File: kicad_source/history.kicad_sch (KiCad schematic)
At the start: 0 parts

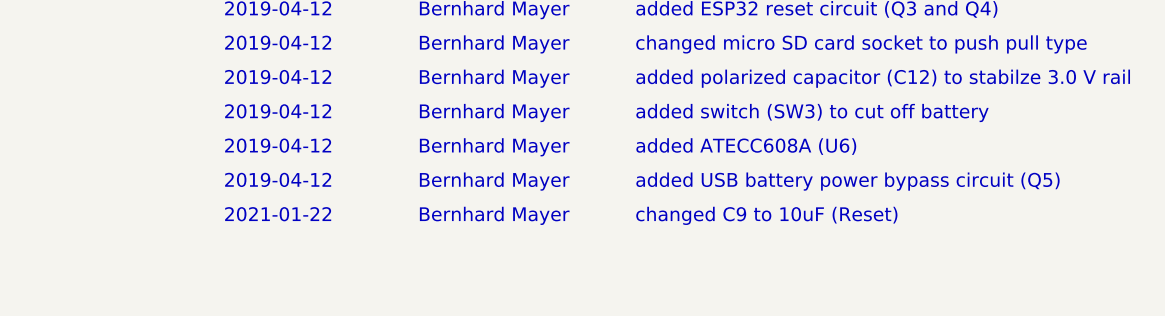
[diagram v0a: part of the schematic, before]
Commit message: added pull up on BOOT
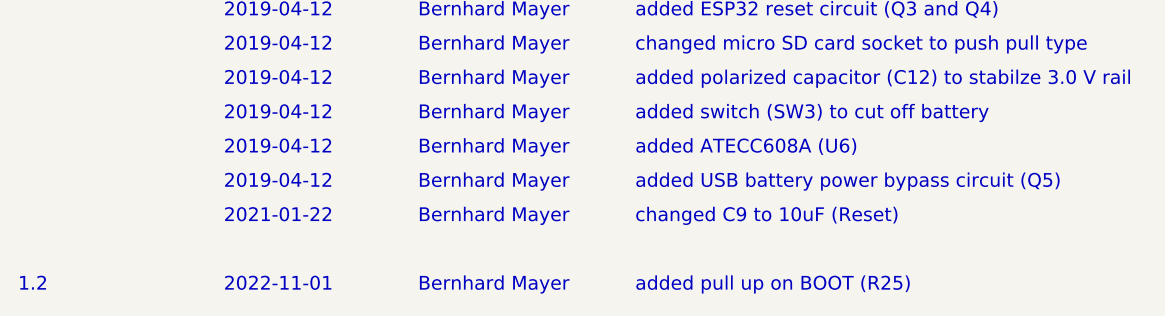
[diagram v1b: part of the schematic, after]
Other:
- note added: "1.2"
- note added: "2022-11-01"
- note added: "added pull up on BOOT (R25)"
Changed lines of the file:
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@@
+    (effects (font (size 1.524 1.524)) (justify left bottom))
+  )
+  (text "Bernhard Mayer" (at 64.77 67.31 0)
     (effects (font (size 1.524 1.524)) (justify left bottom))
   )
@@
     (effects (font (size 1.524 1.524)) (justify left bottom))
   )
+  (text "added pull up on BOOT (R25)" (at 88.9 67.31 0)
+    (effects (font (size 1.524 1.524)) (justify left bottom))
+  )
   (text "Bernhard Mayer" (at 64.77 33.02 0)
     (effects (font (size 1.524 1.524)) (justify left bottom))
@@
     (effects (font (size 1.524 1.524)) (justify left bottom))
   )
+  (text "2022-11-01" (at 43.18 67.31 0)
+    (effects (font (size 1.524 1.524)) (justify left bottom))
+  )
   (text "added switch (SW3) to cut off battery" (at 88.9 48.26 0)
     (effects (font (size 1.524 1.524)) (justify left bottom))
@@
     (effects (font (size 1.524 1.524)) (justify left bottom))
   )
+  (text "1.2" (at 20.32 67.31 0)
+    (effects (font (size 1.524 1.524)) (justify left bottom))
+  )

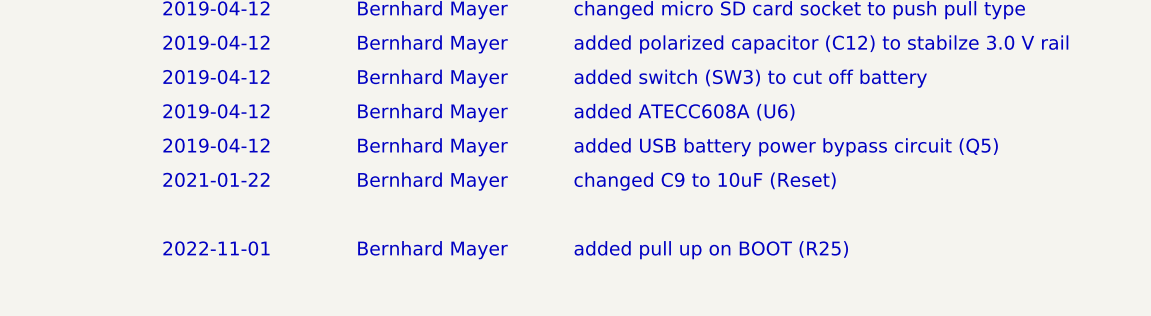
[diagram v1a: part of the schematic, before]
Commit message: added qwiic connector
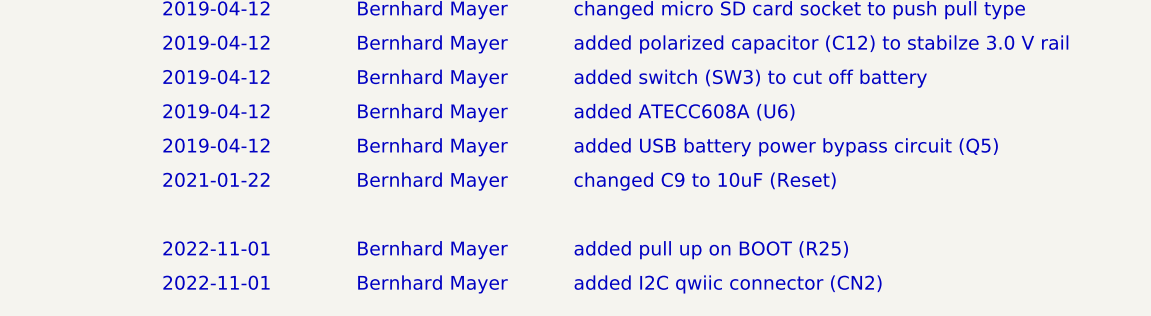
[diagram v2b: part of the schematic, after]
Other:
- note added: "added I2C qwiic connector (CN2)"
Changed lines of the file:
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@@
+    (effects (font (size 1.524 1.524)) (justify left bottom))
+  )
+  (text "2022-11-01" (at 43.18 71.12 0)
     (effects (font (size 1.524 1.524)) (justify left bottom))
   )
@@
     (effects (font (size 1.524 1.524)) (justify left bottom))
   )
+  (text "Bernhard Mayer" (at 64.77 71.12 0)
+    (effects (font (size 1.524 1.524)) (justify left bottom))
+  )
   (text "2019-04-12" (at 43.18 36.83 0)
     (effects (font (size 1.524 1.524)) (justify left bottom))
@@
     (effects (font (size 1.524 1.524)) (justify left bottom))
   )
+  (text "added I2C qwiic connector (CN2)" (at 88.9 71.12 0)
+    (effects (font (size 1.524 1.524)) (justify left bottom))
+  )

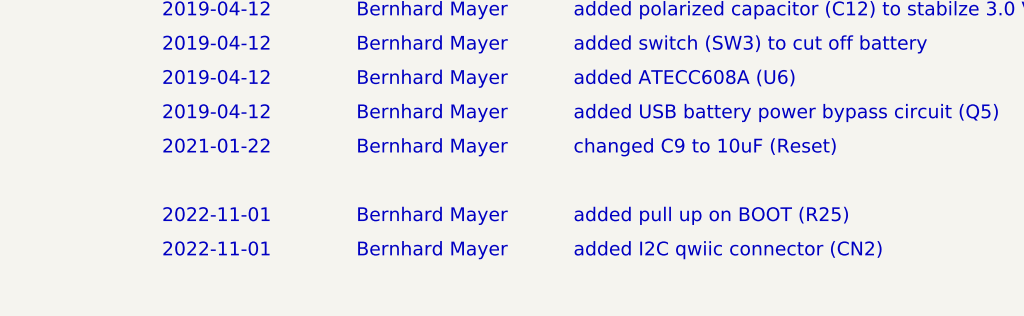
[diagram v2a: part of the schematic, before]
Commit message: added i2c eeprom
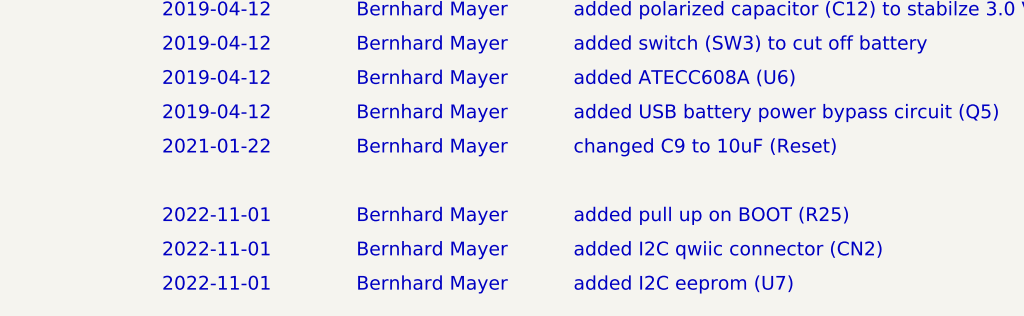
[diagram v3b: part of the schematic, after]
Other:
- note added: "added I2C eeprom (U7)"
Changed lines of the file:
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@@
+    (effects (font (size 1.524 1.524)) (justify left bottom))
+  )
+  (text "added I2C eeprom (U7)" (at 88.9 74.93 0)
     (effects (font (size 1.524 1.524)) (justify left bottom))
   )
@@
     (effects (font (size 1.524 1.524)) (justify left bottom))
   )
+  (text "2022-11-01" (at 43.18 74.93 0)
+    (effects (font (size 1.524 1.524)) (justify left bottom))
+  )
   (text "1.2" (at 20.32 67.31 0)
     (effects (font (size 1.524 1.524)) (justify left bottom))
   )
+  (text "Bernhard Mayer" (at 64.77 74.93 0)
+    (effects (font (size 1.524 1.524)) (justify left bottom))
+  )

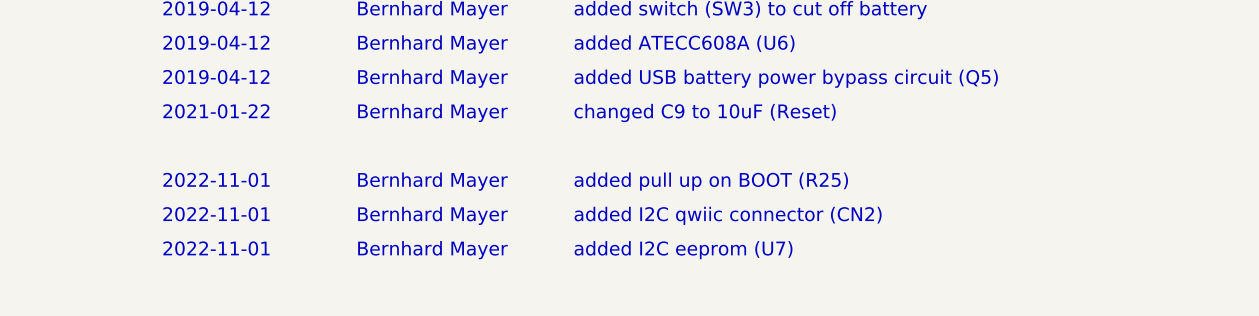
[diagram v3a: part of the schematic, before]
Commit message: added CAN transceiver
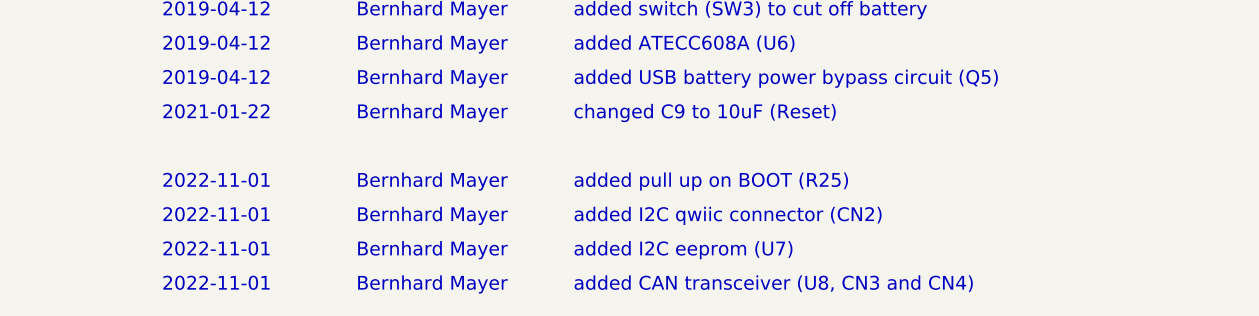
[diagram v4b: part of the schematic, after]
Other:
- note added: "added CAN transceiver (U8, CN3 and CN4)"
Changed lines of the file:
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@@
+    (effects (font (size 1.524 1.524)) (justify left bottom))
+  )
+  (text "added CAN transceiver (U8, CN3 and CN4)" (at 88.9 78.74 0)
     (effects (font (size 1.524 1.524)) (justify left bottom))
   )
@@
     (effects (font (size 1.524 1.524)) (justify left bottom))
   )
+  (text "2022-11-01" (at 43.18 78.74 0)
+    (effects (font (size 1.524 1.524)) (justify left bottom))
+  )
   (text "2019-04-12" (at 43.18 33.02 0)
     (effects (font (size 1.524 1.524)) (justify left bottom))
@@
     (effects (font (size 1.524 1.524)) (justify left bottom))
   )
+  (text "Bernhard Mayer" (at 64.77 78.74 0)
+    (effects (font (size 1.524 1.524)) (justify left bottom))
+  )

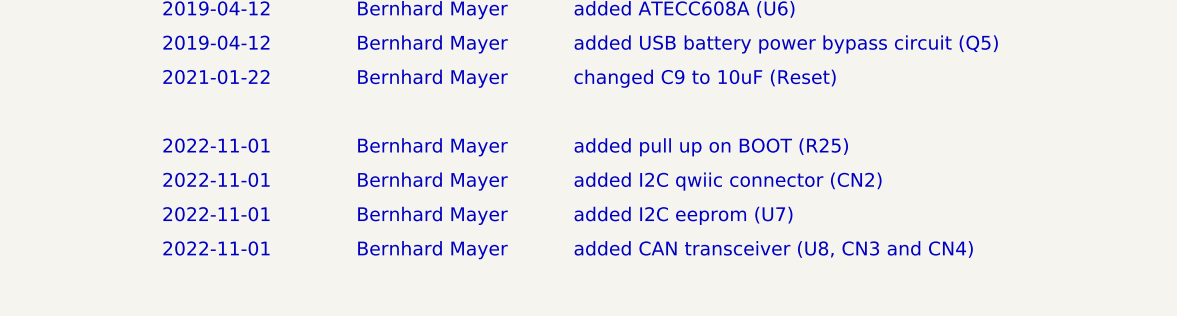
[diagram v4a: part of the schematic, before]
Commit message: added usb c connector
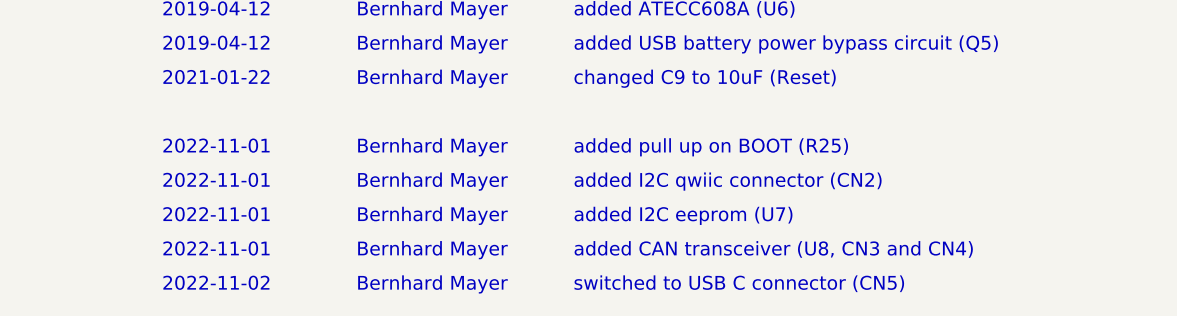
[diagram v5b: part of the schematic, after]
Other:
- note added: "2022-11-02"
- note added: "switched to USB C connector (CN5)"
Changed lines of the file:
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@@
+    (effects (font (size 1.524 1.524)) (justify left bottom))
+  )
+  (text "switched to USB C connector (CN5)" (at 88.9 82.55 0)
     (effects (font (size 1.524 1.524)) (justify left bottom))
   )
@@
   )
   (text "Bernhard Mayer" (at 64.77 55.88 0)
+    (effects (font (size 1.524 1.524)) (justify left bottom))
+  )
+  (text "Bernhard Mayer" (at 64.77 82.55 0)
     (effects (font (size 1.524 1.524)) (justify left bottom))
   )
@@
     (effects (font (size 1.524 1.524)) (justify left bottom))
   )
+  (text "2022-11-02" (at 43.18 82.55 0)
+    (effects (font (size 1.524 1.524)) (justify left bottom))
+  )

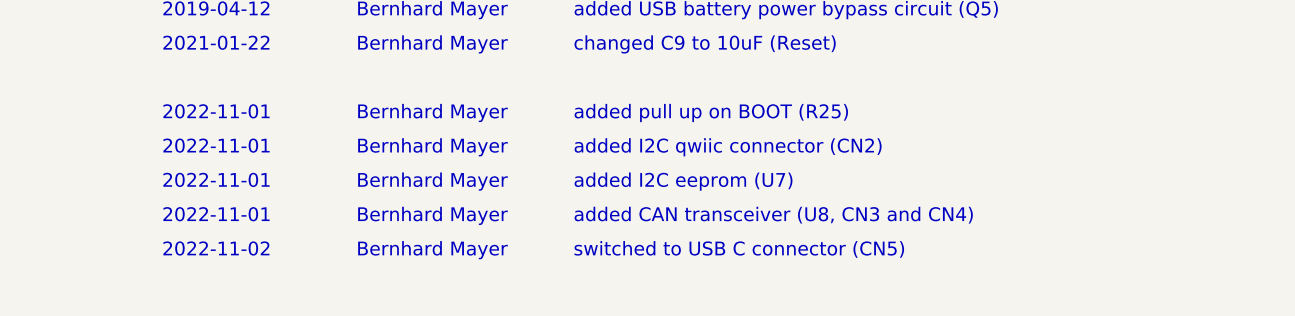
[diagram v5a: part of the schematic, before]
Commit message: added resistors on USB CC
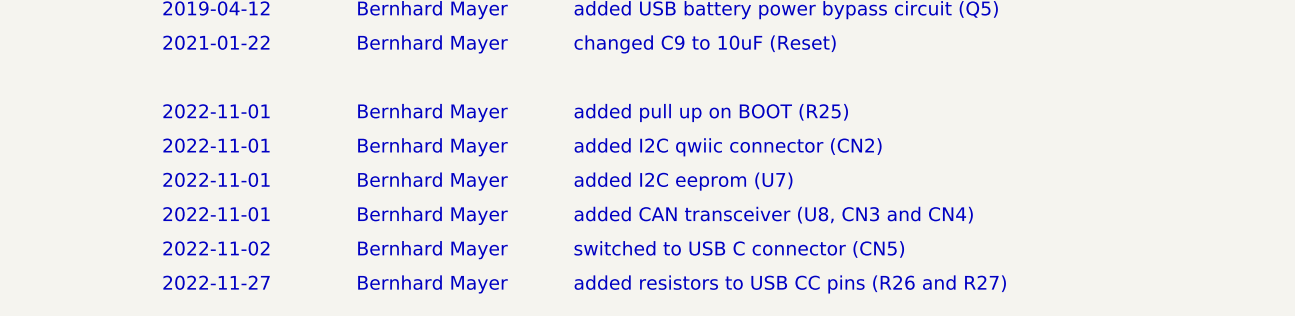
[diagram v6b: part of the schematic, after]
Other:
- note added: "2022-11-27"
- note added: "added resistors to USB CC pins (R26 and R27)"
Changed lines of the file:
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@@
   (title_block
     (title "Sensornator")
-    (date "2022-11-01")
+    (date "2022-11-27")
     (rev "1.2")
     (company "generationmake")
@@
     (effects (font (size 1.524 1.524)) (justify left bottom))
   )
+  (text "Bernhard Mayer" (at 64.77 86.36 0)
+    (effects (font (size 1.524 1.524)) (justify left bottom))
+  )
+  (text "2022-11-27" (at 43.18 86.36 0)
+    (effects (font (size 1.524 1.524)) (justify left bottom))
+  )
   (text "Bernhard Mayer" (at 64.77 33.02 0)
     (effects (font (size 1.524 1.524)) (justify left bottom))
@@
     (effects (font (size 1.524 1.524)) (justify left bottom))
   )
+  (text "added resistors to USB CC pins (R26 and R27)" (at 88.9 86.36 0)
+    (effects (font (size 1.524 1.524)) (justify left bottom))
+  )

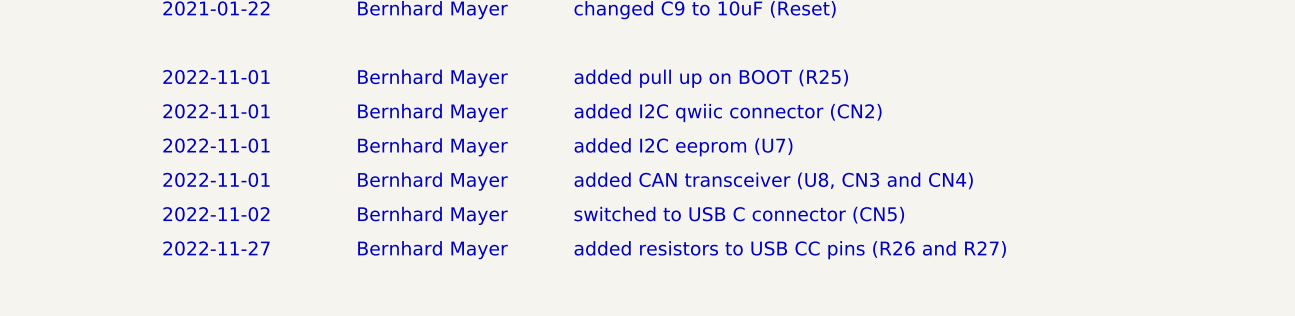
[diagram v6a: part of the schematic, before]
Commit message: added mounting pins on connectors, added labels
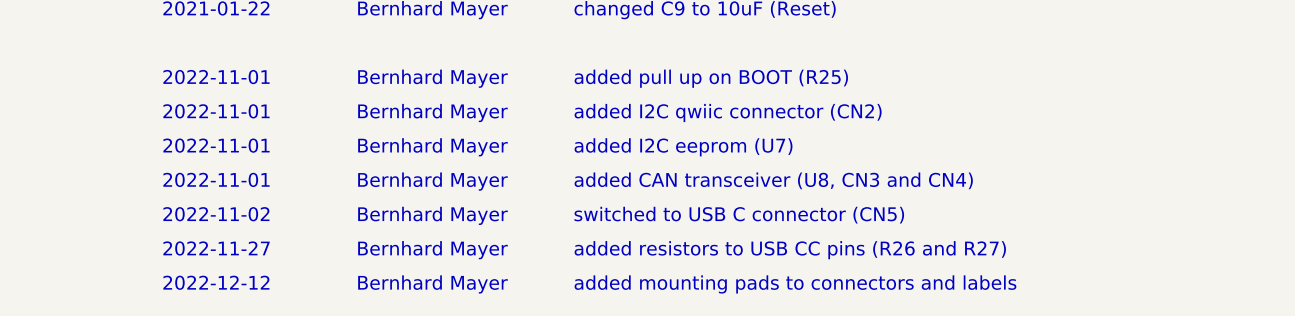
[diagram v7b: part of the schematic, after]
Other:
- note added: "2022-12-12"
- note added: "added mounting pads to connectors and labels"
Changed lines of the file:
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@@
   (title_block
     (title "Sensornator")
-    (date "2022-11-27")
+    (date "2022-12-12")
     (rev "1.2")
     (company "generationmake")
@@
     (effects (font (size 1.524 1.524)) (justify left bottom))
   )
+  (text "2022-12-12" (at 43.18 90.17 0)
+    (effects (font (size 1.524 1.524)) (justify left bottom))
+  )
   (text "Bernhard Mayer" (at 64.77 33.02 0)
     (effects (font (size 1.524 1.524)) (justify left bottom))
@@
     (effects (font (size 1.524 1.524)) (justify left bottom))
   )
+  (text "added mounting pads to connectors and labels" (at 88.9 90.17 0)
+    (effects (font (size 1.524 1.524)) (justify left bottom))
+  )
   (text "added resistors to USB CC pins (R26 and R27)" (at 88.9 86.36 0)
     (effects (font (size 1.524 1.524)) (justify left bottom))
   )
+  (text "Bernhard Mayer" (at 64.77 90.17 0)
+    (effects (font (size 1.524 1.524)) (justify left bottom))
+  )
